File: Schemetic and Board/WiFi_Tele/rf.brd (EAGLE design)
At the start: 49.4 x 52.8 mm, 26 parts

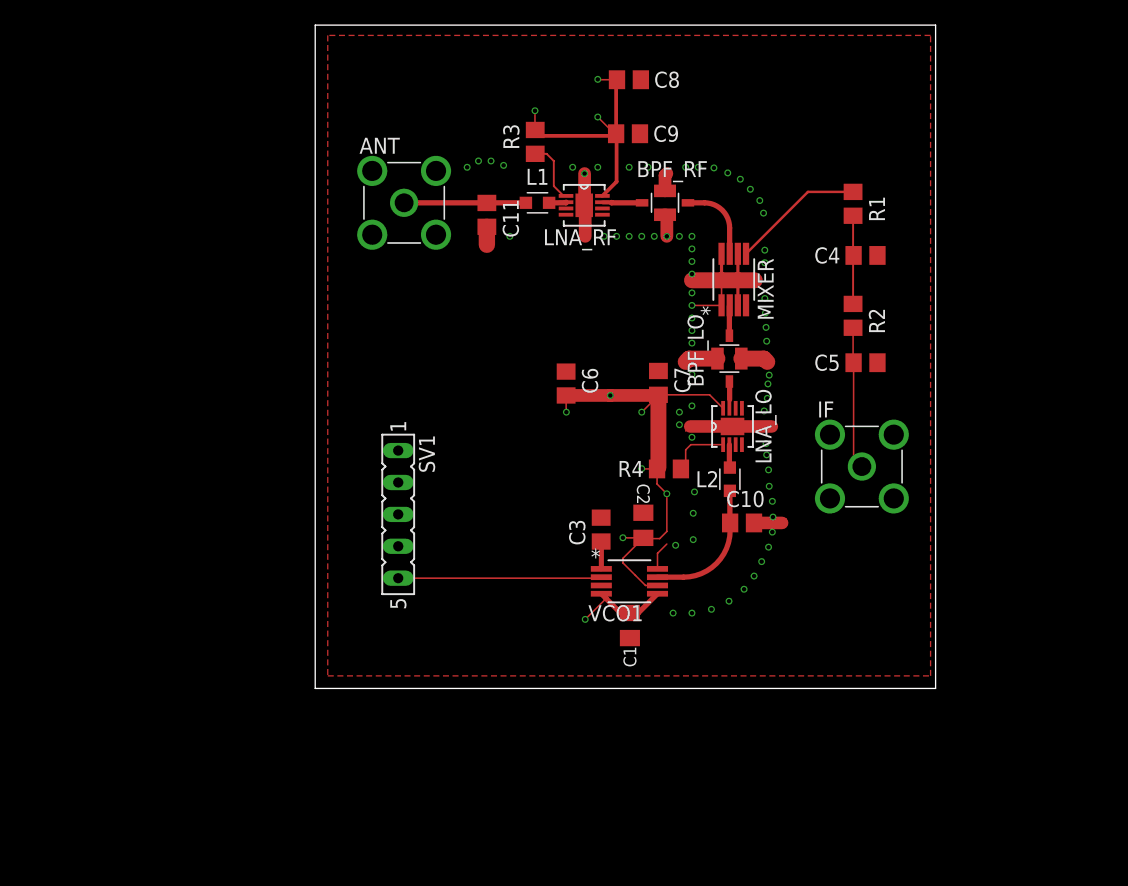
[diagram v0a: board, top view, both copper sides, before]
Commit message: changed mixer
Changed mixer from HMC213B to LT5522 due to stock issues
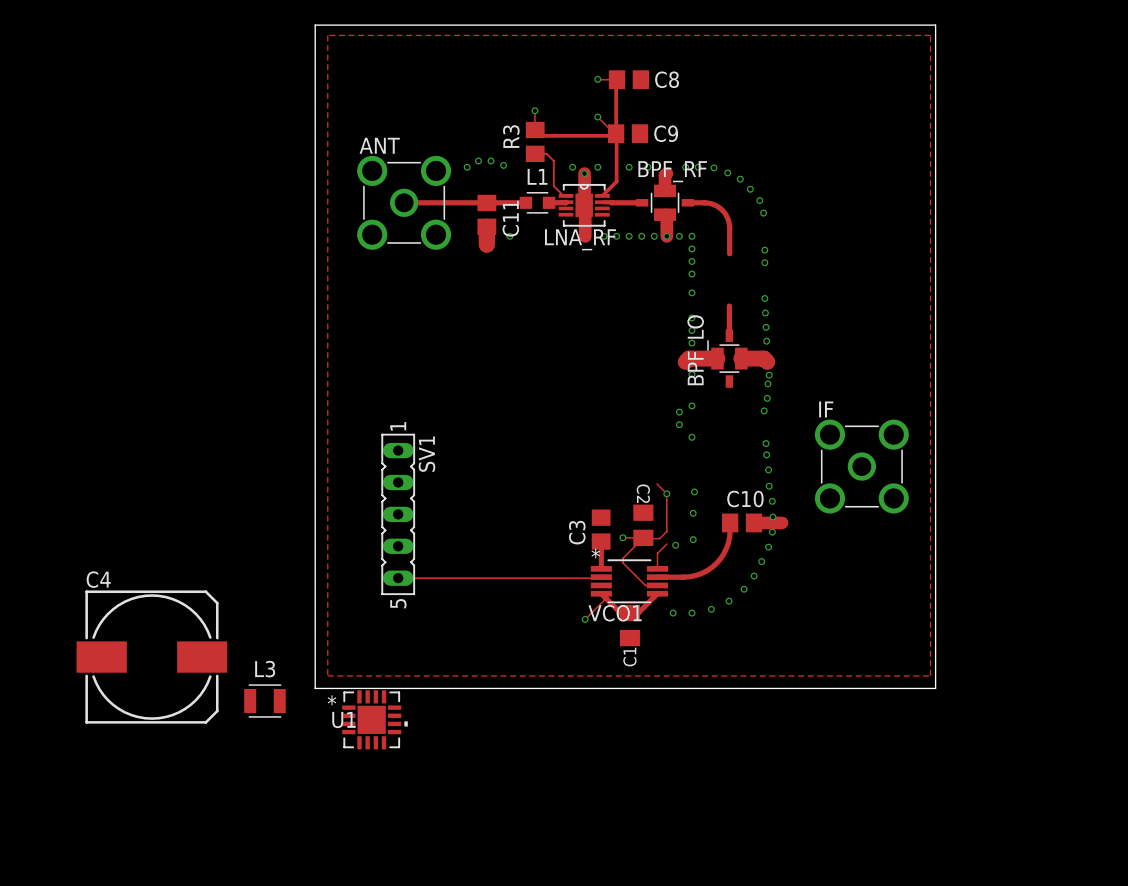
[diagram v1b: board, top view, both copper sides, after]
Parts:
- removed C5: 10pF, rcl:C0805
- removed C6: 100nF, rcl:C0805
- removed C7: 1nF, rcl:C0805
- removed L2: 1nH, Passives:INDC1607X61
- removed LNA_LO: ADL5523ACPZ-R7CP_8_2-M, ADL5523ACPZ-R7:CP_8_2-M
- removed MIXER: HMC213BMS8E, HMC213B:RM_8
- removed R1, R2: 33k, rcl:R0805
- removed R4: 1.33k, rcl:R0805
- added L3: 4.7nH, Passives:INDC2518X180
- added U1: LT5522EUF, LT5522:QFN-16_UF
- C4: value 10pF -> 1000uF; device rcl:C0805 -> rcl:153CLV-1010
- moved C4 65.2 mm to (-13.0, 2.50)
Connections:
- removed net IF: MIXER.5, R1.1
- removed net IF_AA: C5.1, IF.1, R2.2
- removed net N$6: L2.2, LNA_LO.2
- removed net N$7: C10.1, L2.1, VCO1.7
- net 5V: now also C4.+, U1.5, U1.6, U1.7; no longer C6.2, C7.2, LNA_LO.8, R4.2
- net GND: now also C4.-, L3.2, U1.1, U1.12, U1.13, U1.14, U1.16, U1.17, U1.2, U1.4, U1.8, U1.9; no longer C4.2, C5.2, C6.1, C7.1, IF.2, IF.3, IF.4, IF.5, LNA_LO.9, MIXER.1, MIXER.3, MIXER.6, MIXER.8
- net LO_AMPED: now also C10.1, VCO1.7; no longer LNA_LO.7
- net LO_FILTERED: now also U1.15; no longer MIXER.2
- net N$3: now also IF.1, U1.11; no longer LNA_LO.1, R4.1
- net N$4: now also IF.2, IF.3, IF.4, IF.5, U1.10; no longer C4.1, R1.2, R2.1
- net RF_FILTERED: now also L3.1, U1.3; no longer MIXER.7
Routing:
- net GND: track 44.7 -> 20.0 mm, vias 68 -> 67
- net 5V: track 68.2 -> 43.6 mm, vias 10 -> 6
- net IF_AA: track 11.3 -> 0.00 mm
- net IF: track 10.6 -> 0.00 mm
- net N$7: track 10.5 -> 0.00 mm
- net N$4: track 7.56 -> 0.00 mm
- net LO_AMPED: track 2.14 -> 7.93 mm
- net N$3: track 4.83 -> 0.00 mm
- net N$6: track 1.83 -> 0.00 mm

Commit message: rf schematic v2
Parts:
- added C5: 0.01uF, rcl:C0805
- added C6: 3.3uF, rcl:C0805
- added U$1: ETC4-1-2TR, ETC4-1-2TR:SM-22
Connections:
- new net N$6: U$1.1, U1.11
- new net N$7: IF.2, IF.3, IF.4, IF.5, U$1.4
- net 5V: now also C5.1, C6.1, U$1.2
- net GND: now also C5.2, C6.2, SV1.1, SV1.3, SV1.5; no longer SV1.4
- net N$3: now also U$1.5; no longer U1.11
- net N$4: now also U$1.3; no longer IF.2, IF.3, IF.4, IF.5
- net VCO_TUNE: now also SV1.4; no longer SV1.5
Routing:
- net VCO_TUNE: track 16.2 -> 0.11 mm
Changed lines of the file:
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@@
 <drawing>
 <settings>
-<setting alwaysvectorfont="yes"/>
+<setting alwaysvectorfont="no"/>
 <setting verticaltext="up"/>
 </settings>
@@
 <attribute name="SPICEPREFIX" value="C" x="-13" y="2.5" size="1.778" layer="27" display="off"/>
 </element>
+<element name="U$1" library="ETC4-1-2TR" package="SM-22" value="ETC4-1-2TR" x="-22.5" y="-4"/>
+<element name="C5" library="rcl" library_urn="urn:adsk.eagle:library:334" package="C0805" package3d_urn="urn:adsk.eagle:package:23617/2" value="0.01uF" x="-21.5" y="-8.5">
+<attribute name="SPICEPREFIX" value="C" x="-21.5" y="-8.5" size="1.778" layer="27" display="off"/>
+</element>
+<element name="C6" library="rcl" library_urn="urn:adsk.eagle:library:334" package="C0805" package3d_urn="urn:adsk.eagle:package:23617/2" value="3.3uF" x="-21.5" y="-13">
+<attribute name="SPICEPREFIX" value="C" x="-21.5" y="-13" size="1.778" layer="27" display="off"/>
+</element>
 </elements>
 <signals>
@@
 <contactref element="ANT" pad="4"/>
 <contactref element="ANT" pad="5"/>
-<contactref element="SV1" pad="4"/>
 <polygon width="0.1524" layer="2">
 <vertex x="1" y="52"/>
@@
 <contactref element="U1" pad="14"/>
 <contactref element="C4" pad="-"/>
+<contactref element="SV1" pad="5"/>
+<contactref element="SV1" pad="3"/>
+<contactref element="SV1" pad="1"/>
+<contactref element="C6" pad="2"/>
+<contactref element="C5" pad="2"/>
 <wire x1="25.86" y1="44.17" x2="25.93" y2="48.47" width="0" layer="19" extent="1-1"/>
 <wire x1="26.5" y1="41.5" x2="25.86" y2="44.17" width="0" layer="19" extent="1-1"/>
@@
 <wire x1="4.54" y1="41.21" x2="9.62" y2="41.21" width="0" layer="19" extent="1-1"/>
 <wire x1="4.54" y1="36.13" x2="9.62" y2="36.13" width="0" layer="19" extent="1-1"/>
-<wire x1="6.61" y1="11.32" x2="22.77" y2="13.6" width="0" layer="19" extent="1-1"/>
-<wire x1="5.475" y1="-0.672603125" x2="6.61" y2="11.32" width="0" layer="19" extent="1-1"/>
+<wire x1="6.61" y1="13.86" x2="22.77" y2="13.6" width="0" layer="19" extent="1-1"/>
+<wire x1="6.61" y1="18.94" x2="6.61" y2="13.86" width="0" layer="19" extent="1-1"/>
+<wire x1="6.61" y1="8.78" x2="6.61" y2="13.86" width="0" layer="19" extent="1-1"/>
+<wire x1="5.475" y1="-0.672603125" x2="6.61" y2="8.78" width="0" layer="19" extent="1-1"/>
 <wire x1="4.825" y1="-0.672603125" x2="5.475" y2="-0.672603125" width="0" layer="19" extent="1-1"/>
 <wire x1="6.327396875" y1="-1.525" x2="5.475" y2="-0.672603125" width="0" layer="19" extent="1-1"/>
@@
 <wire x1="-2.825" y1="-1" x2="2.672603125" y2="-1.525" width="0" layer="19" extent="1-1"/>
 <wire x1="-17" y1="2.5" x2="-2.825" y2="-1" width="0" layer="19" extent="1-1"/>
+<wire x1="-20.55" y1="-8.5" x2="-17" y2="2.5" width="0" layer="19" extent="1-1"/>
+<wire x1="-20.55" y1="-13" x2="-20.55" y2="-8.5" width="0" layer="19" extent="1-1"/>
 </signal>
 <signal name="N$2">
@@
 <signal name="VCO_TUNE">
 <contactref element="VCO1" pad="2"/>
-<contactref element="SV1" pad="5"/>
-<wire x1="6.61" y1="8.78" x2="22.7046" y2="8.78" width="0.127" layer="1"/>
 <wire x1="22.7046" y1="8.78" x2="22.7848" y2="8.8602" width="0.127" layer="1"/>
+<contactref element="SV1" pad="4"/>
+<wire x1="6.61" y1="11.32" x2="22.7046" y2="8.78" width="0" layer="19" extent="1-1"/>
 </signal>
 <signal name="LO_AMPED" class="1">
@@
 <contactref element="U1" pad="5"/>
 <contactref element="C4" pad="+"/>
+<contactref element="U$1" pad="2"/>
+<contactref element="C5" pad="1"/>
+<contactref element="C6" pad="1"/>
 <wire x1="27.22" y1="16.28" x2="22.8678" y2="39.22" width="0" layer="19" extent="1-1"/>
 <wire x1="27.2552" y1="7.5394" x2="27.2552" y2="8.1998" width="0" layer="19" extent="1-1"/>
@@
 <wire x1="3.525" y1="-4.327396875" x2="4.175" y2="-4.327396875" width="0" layer="19" extent="1-1"/>
 <wire x1="-9" y1="2.5" x2="3.525" y2="-4.327396875" width="0" layer="19" extent="1-1"/>
+<wire x1="-21.23" y1="-0.57" x2="-9" y2="2.5" width="0" layer="19" extent="1-1"/>
+<wire x1="-22.45" y1="-8.5" x2="-21.23" y2="-0.57" width="0" layer="19" extent="1-1"/>
+<wire x1="-22.45" y1="-13" x2="-22.45" y2="-8.5" width="0" layer="19" extent="1-1"/>
 </signal>
 <signal name="N$1">
@@
 <wire x1="13.67" y1="38.67" x2="13.67" y2="38.66" width="0.41896875" layer="1"/>
 </signal>
-<signal name="N$3">
-<contactref element="U1" pad="11"/>
-<contactref element="IF" pad="1"/>
-<wire x1="6.327396875" y1="-2.175" x2="43.53" y2="17.67" width="0" layer="19" extent="1-1"/>
-</signal>
 <signal name="N$4">
 <contactref element="U1" pad="10"/>
-<contactref element="IF" pad="3"/>
-<contactref element="IF" pad="4"/>
+<contactref element="U$1" pad="3"/>
+<wire x1="6.327396875" y1="-2.825" x2="-19.96" y2="-0.57" width="0" layer="19" extent="1-1"/>
+</signal>
+<signal name="N$6">
+<contactref element="U1" pad="11"/>
+<contactref element="U$1" pad="1"/>
+<wire x1="6.327396875" y1="-2.175" x2="-22.5" y2="-0.57" width="0" layer="19" extent="1-1"/>
+</signal>
+<signal name="N$3">
+<contactref element="U$1" pad="5"/>
+<contactref element="IF" pad="1"/>
+<wire x1="-19.96" y1="-4" x2="43.53" y2="17.67" width="0" layer="19" extent="1-1"/>
+</signal>
+<signal name="N$7">
+<contactref element="U$1" pad="4"/>
 <contactref element="IF" pad="2"/>
 <contactref element="IF" pad="5"/>
+<contactref element="IF" pad="4"/>
+<contactref element="IF" pad="3"/>
 <wire x1="40.99" y1="20.21" x2="46.07" y2="20.21" width="0" layer="19" extent="1-1"/>
 <wire x1="46.07" y1="15.13" x2="46.07" y2="20.21" width="0" layer="19" extent="1-1"/>
 <wire x1="40.99" y1="15.13" x2="40.99" y2="20.21" width="0" layer="19" extent="1-1"/>
-<wire x1="6.327396875" y1="-2.825" x2="40.99" y2="15.13" width="0" layer="19" extent="1-1"/>
+<wire x1="-22.5" y1="-4" x2="40.99" y2="15.13" width="0" layer="19" extent="1-1"/>
 </signal>
 </signals>

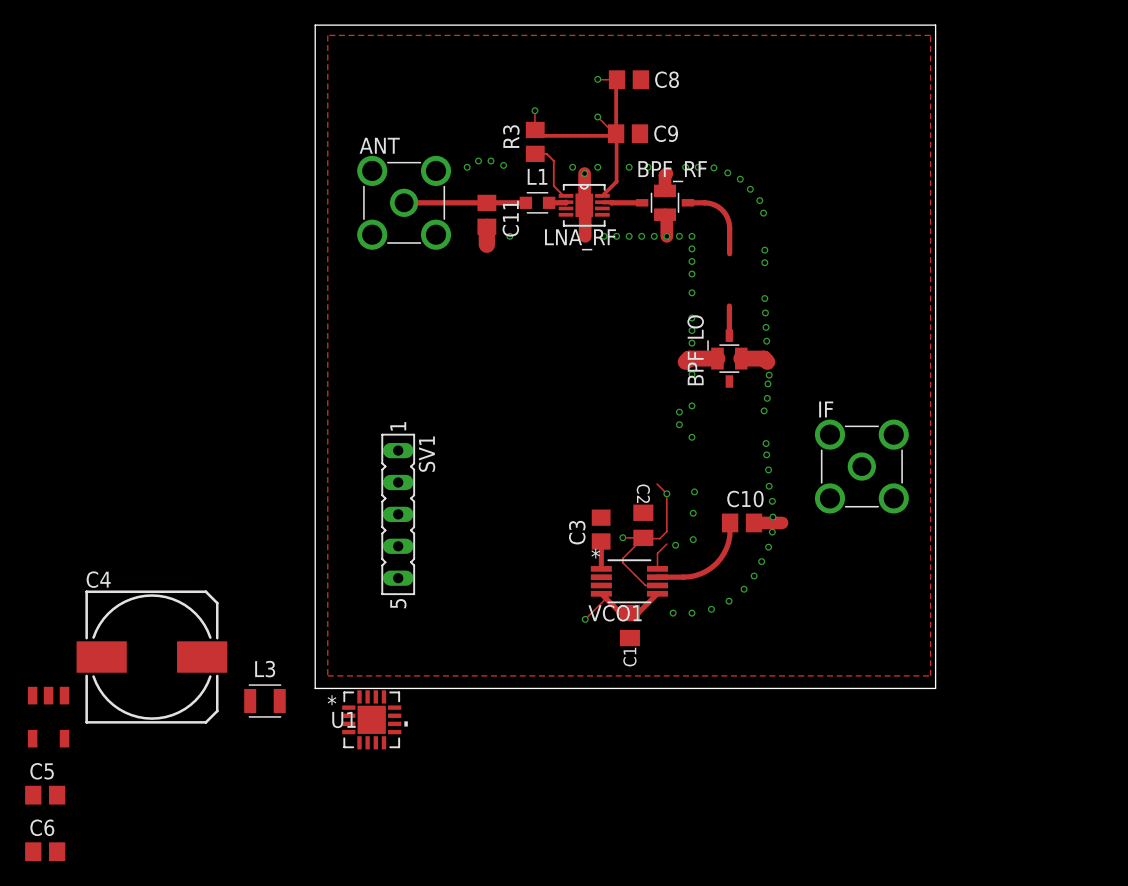
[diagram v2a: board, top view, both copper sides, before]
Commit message: Start FPGA board routing
Routed SMA -> VGA1 matched diff pairs
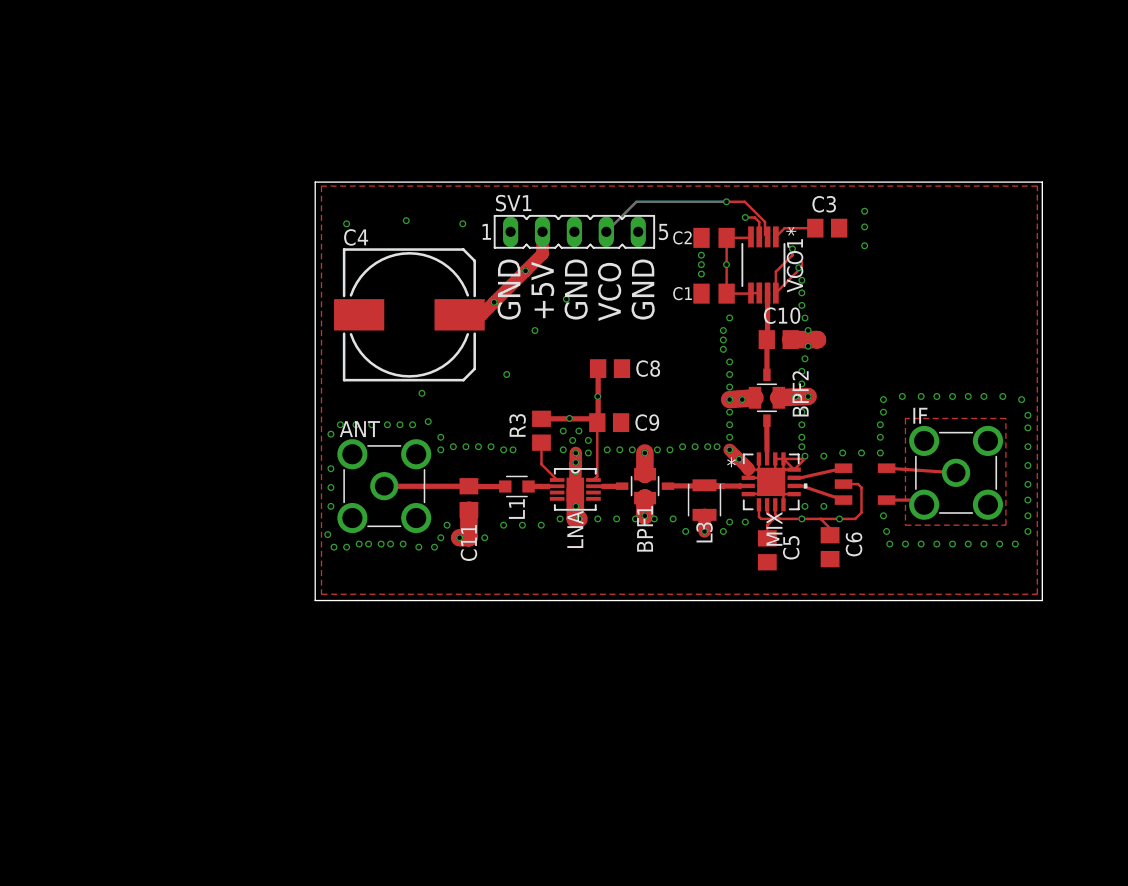
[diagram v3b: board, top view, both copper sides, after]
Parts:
- removed BPF_LO, BPF_RF: 2450BP18C100C, Johanson BPF 2450BP18C100C:SMD
- removed LNA_RF: ADL5523ACPZ-R7CP_8_2-M, ADL5523ACPZ-R7:CP_8_2-M
- removed U1: LT5522EUF, LT5522:QFN-16_UF
- added BPF1, BPF2: 2450BP18C100C, Johanson BPF 2450BP18C100C:SMD
- added LNA: ADL5523ACPZ-R7CP_8_2-M, ADL5523ACPZ-R7:CP_8_2-M
- added MIX: LT5522EUF, LT5522:QFN-16_UF
- moved U$1 70.6 mm to (45.5, 15.0), turned to 90 degrees
- moved C6 67.0 mm to (41.0, 11.2), turned to 270 degrees
- moved C5 60.7 mm to (36.0, 11.0), turned to 270 degrees
- moved L3 38.5 mm to (31.0, 15.0), turned to 270 degrees
- moved C4 34.1 mm to (7.50, 29.8)
- moved C3 30.0 mm to (40.8, 36.6), turned to 0 degrees
- moved VCO1 27.4 mm to (35.7, 33.7), turned to 270 degrees
- moved C1 27.3 mm to (31.8, 31.4), turned to 180 degrees
- moved SV1 26.5 mm to (20.6, 36.4), turned to 0 degrees
- moved C2 23.6 mm to (31.8, 35.9), turned to 180 degrees
- moved C8 23.0 mm to (23.5, 25.5)
- moved C9 23.0 mm to (23.4, 21.2)
- moved R3 23.0 mm to (18.0, 20.5)
- moved L1 22.6 mm to (16.1, 16.1)
- moved ANT 22.6 mm to (5.50, 16.1)
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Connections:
- net N$3 renamed IF+
- net N$7 renamed IF-
- removed net N$6: U$1.1, U1.11
- new net IF_P: MIX.11, U$1.3
- net 5V: now also LNA.8, MIX.5, MIX.6, MIX.7; no longer LNA_RF.8, U1.5, U1.6, U1.7
- net GND: now also BPF1.GND$1, BPF1.GND$2, BPF2.GND$1, BPF2.GND$2, LNA.9, MIX.1, MIX.12, MIX.13, MIX.14, MIX.16, MIX.17, MIX.2, MIX.4, MIX.8, MIX.9; no longer BPF_LO.GND$1, BPF_LO.GND$2, BPF_RF.GND$1, BPF_RF.GND$2, LNA_RF.9, U1.1, U1.12, U1.13, U1.14, U1.16, U1.17, U1.2, U1.4, U1.8, U1.9
- net LO_AMPED: now also BPF2.I/O$1; no longer BPF_LO.I/O$1
- net LO_FILTERED: now also BPF2.I/O$2, MIX.15; no longer BPF_LO.I/O$2, U1.15
- net N$1: now also LNA.1; no longer LNA_RF.1
- net N$4: now also MIX.10, U$1.1; no longer U$1.3, U1.10
- net N$5: now also LNA.2; no longer LNA_RF.2
- net RF_AMPED: now also BPF1.I/O$1, LNA.7; no longer BPF_RF.I/O$1, LNA_RF.7
- net RF_FILTERED: now also BPF1.I/O$2, MIX.3; no longer BPF_RF.I/O$2, U1.3
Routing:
- net GND: track 20.0 -> 56.6 mm, vias 67 -> 152
- net VCO_TUNE: track 0.11 -> 15.6 mm, vias 0 -> 1
- net 5V: track 43.6 -> 54.0 mm, vias 6 -> 7
- net IF+: track 0.00 -> 5.54 mm
- net N$4: track 0.00 -> 4.12 mm
- net IF_P: track 0.00 -> 4.02 mm
- net IF-: track 0.00 -> 3.14 mm
- net RF_FILTERED: track 6.20 -> 7.95 mm
- net N$1: track 5.01 -> 3.48 mm
- net LO_AMPED: track 7.93 -> 6.63 mm
- net N$2: track 2.19 -> 3.43 mm
- net RF_AMPED: track 3.20 -> 2.29 mm
- net N$5: track 1.40 -> 2.29 mm
- net LO_FILTERED: track 2.39 -> 3.05 mm
- added copper zone on layer 1, net IF-
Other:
- board size 49.4 x 52.8 mm -> 57.9 x 33.3 mm
- board text added: "GND +5V GND VCO GND"

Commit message: board complete and send for manufacturing
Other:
- board text added: "PA WiFi RF Alistair Symonds"
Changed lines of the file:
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@@
 <drawing>
 <settings>
-<setting alwaysvectorfont="no"/>
+<setting alwaysvectorfont="yes"/>
 <setting verticaltext="up"/>
 </settings>
@@
 VCO
 GND</text>
+<text x="44" y="23.25" size="1.778" layer="25" rot="R45">PA WiFi RF
+Alistair Symonds</text>
 </plain>
 <attributes>

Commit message: Deleted a whole bunch of stuff which shouldn't be in the repo
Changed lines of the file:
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@@
 <?xml version="1.0" encoding="utf-8"?>
 <!DOCTYPE eagle SYSTEM "eagle.dtd">
-<eagle version="9.1.2">
+<eagle version="9.1.3">
 <drawing>
 <settings>
-<setting alwaysvectorfont="yes"/>
+<setting alwaysvectorfont="no"/>
 <setting verticaltext="up"/>
 </settings>
@@
 </polygon>
 <contactref element="LNA" pad="9"/>
-<polygon width="0.127" layer="1" rank="6">
+<polygon width="0.127" layer="1" isolate="0.254" rank="6">
 <vertex x="0.5" y="40"/>
 <vertex x="0.5" y="7.5"/>
@@
 <contactref element="BPF2" pad="I/O$2"/>
 <contactref element="MIX" pad="15"/>
-<wire x1="35.975" y1="18.287396875" x2="35.975" y2="18.9" width="0.2032" layer="1"/>
-<wire x1="35.975" y1="18.9" x2="35.9600625" y2="21.3100625" width="0.41896875" layer="1"/>
-<wire x1="35.9600625" y1="21.3100625" x2="35.97" y2="21.32" width="0.41896875" layer="1"/>
-<wire x1="35.985" y1="18.277396875" x2="35.975" y2="18.287396875" width="0.2032" layer="1"/>
+<wire x1="35.985" y1="18.277396875" x2="35.985" y2="18.89" width="0.2032" layer="1"/>
+<wire x1="35.985" y1="18.89" x2="35.969940625" y2="21.32" width="0.41896875" layer="1"/>
+<wire x1="35.970184375" y1="21.32" x2="35.97" y2="21.32" width="0.41896875" layer="1"/>
+<wire x1="35.970184375" y1="21.32" x2="35.969940625" y2="21.32" width="0.41896875" layer="1"/>
 </signal>
 <signal name="5V">
